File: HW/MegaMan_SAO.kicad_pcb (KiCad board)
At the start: 2 copper layers, 77.5 x 60 mm, 16 parts, among them X1 Badgelife_sao_connector_v169b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

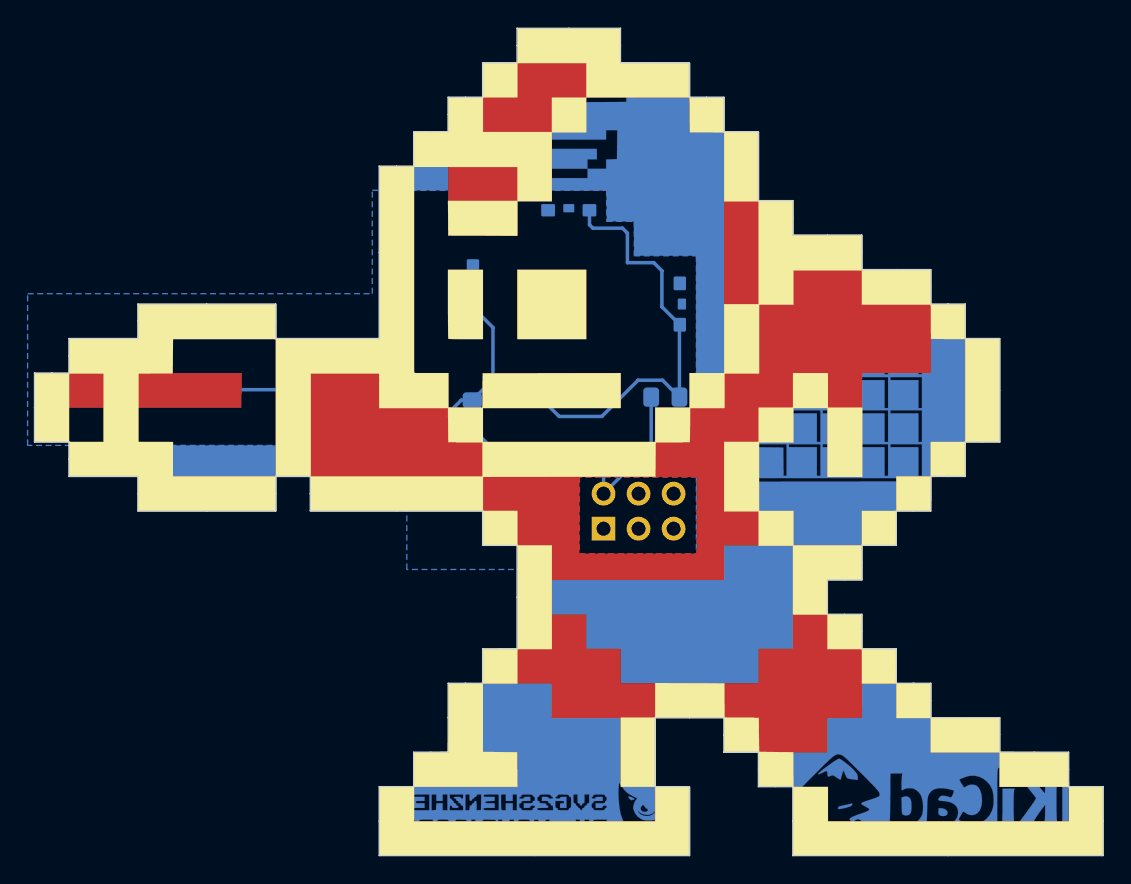
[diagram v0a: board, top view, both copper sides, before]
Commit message: Added Gerbers fixed the blaster LED anode short to ground on F.Cu
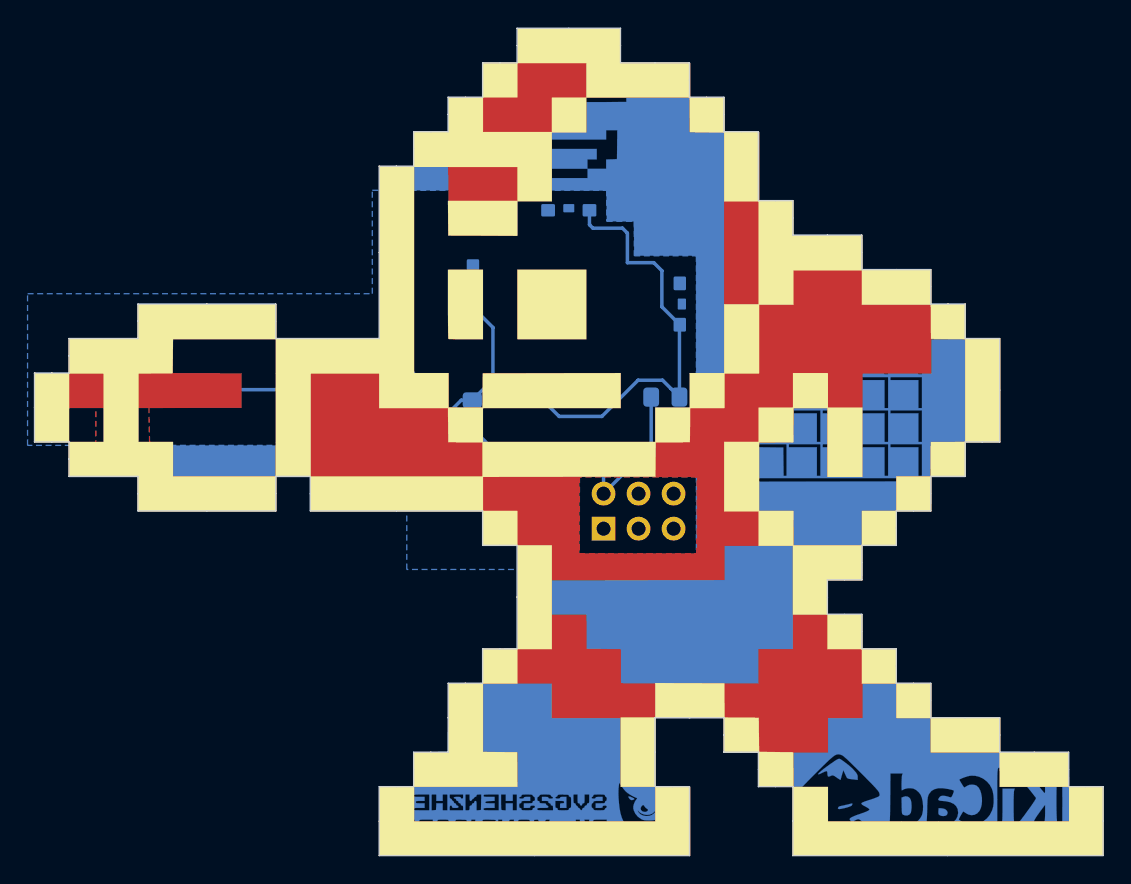
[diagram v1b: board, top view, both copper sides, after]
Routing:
- net Net-(D4-Pad2): track 19.8 -> 16.3 mm
- added copper zone on F.Cu, net (none)
